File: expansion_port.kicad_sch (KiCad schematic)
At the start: 1 part, among them J2 Conn_02x30_Odd_Even

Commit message: rearrange components for routing
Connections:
- net Q3: no longer names the net of J2.35 (Pin_35)
- net Q4: no longer names the net of J2.37 (Pin_37)
- net Q5: no longer names the net of J2.39 (Pin_39)
- net Q6: no longer names the net of J2.41 (Pin_41)
- net Q7: no longer names the net of J2.43 (Pin_43)
- no-connect marks 9 -> 14
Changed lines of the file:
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@@
   (no_connect (at 78.994 36.576))
   (no_connect (at 56.134 36.576))
+  (no_connect (at 66.294 36.576))
+  (no_connect (at 68.834 36.576))
+  (no_connect (at 58.674 36.576))
+  (no_connect (at 61.214 36.576))
+  (no_connect (at 63.754 36.576))
   (no_connect (at 45.974 36.576))
   (no_connect (at 106.934 36.576))
@@
     )
   )
-  (global_label "Q6" (shape input) (at 61.214 36.576 90) (fields_autoplaced)
-    (effects (font (size 1.27 1.27)) (justify left))
-    (property "Intersheet References" "${INTERSHEET_REFS}" (id 0) (at 61.2934 31.6229 90)
-      (effects (font (size 1.27 1.27)) (justify left) hide)
-    )
-  )
   (global_label "~{E}" (shape input) (at 104.394 36.576 90) (fields_autoplaced)
     (effects (font (size 1.27 1.27)) (justify left))
@@
     )
   )
-  (global_label "Q5" (shape input) (at 63.754 36.576 90) (fields_autoplaced)
-    (effects (font (size 1.27 1.27)) (justify left))
-    (property "Intersheet References" "${INTERSHEET_REFS}" (id 0) (at 63.8334 31.6229 90)
-      (effects (font (size 1.27 1.27)) (justify left) hide)
-    )
-  )
   (global_label "~{DMA}" (shape input) (at 53.594 36.576 90) (fields_autoplaced)
     (effects (font (size 1.27 1.27)) (justify left))
@@
     )
   )
-  (global_label "Q3" (shape input) (at 68.834 36.576 90) (fields_autoplaced)
-    (effects (font (size 1.27 1.27)) (justify left))
-    (property "Intersheet References" "${INTERSHEET_REFS}" (id 0) (at 68.9134 31.6229 90)
-      (effects (font (size 1.27 1.27)) (justify left) hide)
-    )
-  )
   (global_label "~{NMI}" (shape input) (at 53.594 49.276 270) (fields_autoplaced)
     (effects (font (size 1.27 1.27)) (justify right))
@@
     )
   )
-  (global_label "Q4" (shape input) (at 66.294 36.576 90) (fields_autoplaced)
-    (effects (font (size 1.27 1.27)) (justify left))
-    (property "Intersheet References" "${INTERSHEET_REFS}" (id 0) (at 66.3734 31.6229 90)
-      (effects (font (size 1.27 1.27)) (justify left) hide)
-    )
-  )
   (global_label "A13" (shape input) (at 66.294 49.276 270) (fields_autoplaced)
     (effects (font (size 1.27 1.27)) (justify right))
@@
       (effects (font (size 1.27 1.27)) (justify left) hide)
     )
-  )
-  (global_label "Q7" (shape input) (at 58.674 36.576 90) (fields_autoplaced)
-    (effects (font (size 1.27 1.27)) (justify left))
-    (property "Intersheet References" "${INTERSHEET_REFS}" (id 0) (at 58.7534 31.6229 90)
-      (effects (font (size 1.27 1.27)) (justify left) hide)
-    )

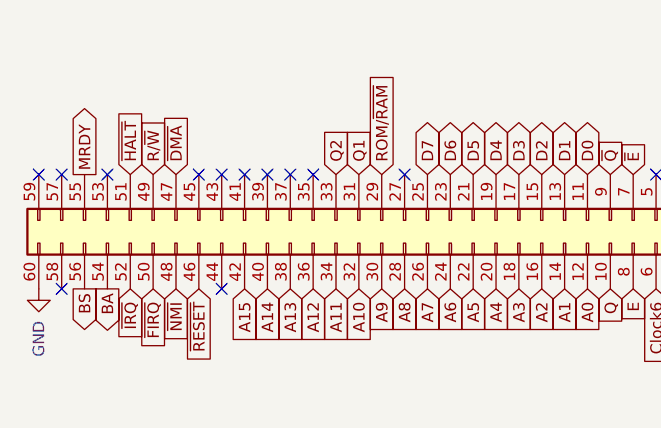
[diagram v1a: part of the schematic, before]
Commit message: correct memory page addressing
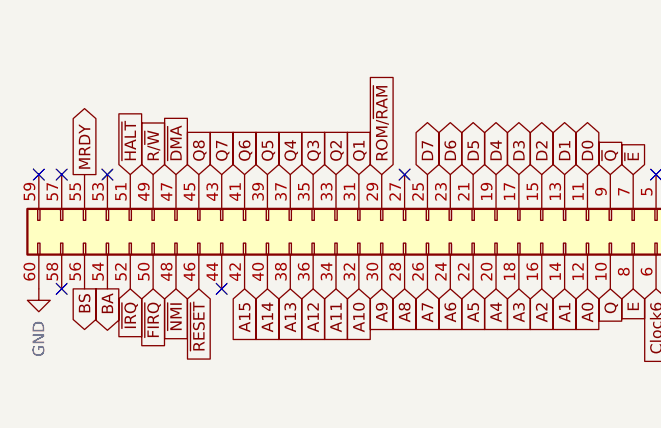
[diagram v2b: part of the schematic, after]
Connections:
- net Q3: now reaches J2.35 (Pin_35)
- net Q4: now reaches J2.37 (Pin_37)
- net Q5: now reaches J2.39 (Pin_39)
- net Q6: now reaches J2.41 (Pin_41)
- net Q7: now reaches J2.43 (Pin_43)
- net Q8: now reaches J2.45 (Pin_45)
- no-connect marks 14 -> 8
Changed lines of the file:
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@@
   (no_connect (at 112.014 36.576))
   (no_connect (at 78.994 36.576))
-  (no_connect (at 56.134 36.576))
-  (no_connect (at 66.294 36.576))
-  (no_connect (at 68.834 36.576))
-  (no_connect (at 58.674 36.576))
-  (no_connect (at 61.214 36.576))
-  (no_connect (at 63.754 36.576))
   (no_connect (at 45.974 36.576))
   (no_connect (at 106.934 36.576))
@@
     )
   )
+  (global_label "Q7" (shape input) (at 58.674 36.576 90) (fields_autoplaced)
+    (effects (font (size 1.27 1.27)) (justify left))
+    (property "Intersheet References" "${INTERSHEET_REFS}" (id 0) (at 58.5946 31.6229 90)
+      (effects (font (size 1.27 1.27)) (justify left) hide)
+    )
+  )
   (global_label "~{Q}" (shape input) (at 101.854 36.576 90) (fields_autoplaced)
     (effects (font (size 1.27 1.27)) (justify left))
@@
     )
   )
+  (global_label "Q4" (shape input) (at 66.294 36.576 90) (fields_autoplaced)
+    (effects (font (size 1.27 1.27)) (justify left))
+    (property "Intersheet References" "${INTERSHEET_REFS}" (id 0) (at 66.2146 31.6229 90)
+      (effects (font (size 1.27 1.27)) (justify left) hide)
+    )
+  )
   (global_label "~{DMA}" (shape input) (at 53.594 36.576 90) (fields_autoplaced)
     (effects (font (size 1.27 1.27)) (justify left))
@@
     )
   )
+  (global_label "Q8" (shape input) (at 56.134 36.576 90) (fields_autoplaced)
+    (effects (font (size 1.27 1.27)) (justify left))
+    (property "Intersheet References" "${INTERSHEET_REFS}" (id 0) (at 56.0546 31.6229 90)
+      (effects (font (size 1.27 1.27)) (justify left) hide)
+    )
+  )
   (global_label "A3" (shape input) (at 91.694 49.276 270) (fields_autoplaced)
     (effects (font (size 1.27 1.27)) (justify right))
@@
     )
   )
+  (global_label "Q6" (shape input) (at 61.214 36.576 90) (fields_autoplaced)
+    (effects (font (size 1.27 1.27)) (justify left))
+    (property "Intersheet References" "${INTERSHEET_REFS}" (id 0) (at 61.1346 31.6229 90)
+      (effects (font (size 1.27 1.27)) (justify left) hide)
+    )
+  )
   (global_label "A7" (shape input) (at 81.534 49.276 270) (fields_autoplaced)
     (effects (font (size 1.27 1.27)) (justify right))
@@
     )
   )
+  (global_label "Q3" (shape input) (at 68.834 36.576 90) (fields_autoplaced)
+    (effects (font (size 1.27 1.27)) (justify left))
+    (property "Intersheet References" "${INTERSHEET_REFS}" (id 0) (at 68.7546 31.6229 90)
+      (effects (font (size 1.27 1.27)) (justify left) hide)
+    )
+  )
   (global_label "A14" (shape input) (at 63.754 49.276 270) (fields_autoplaced)
     (effects (font (size 1.27 1.27)) (justify right))
@@
     )
   )
+  (global_label "Q5" (shape input) (at 63.754 36.576 90) (fields_autoplaced)
+    (effects (font (size 1.27 1.27)) (justify left))
+    (property "Intersheet References" "${INTERSHEET_REFS}" (id 0) (at 63.6746 31.6229 90)
+      (effects (font (size 1.27 1.27)) (justify left) hide)
+    )
+  )

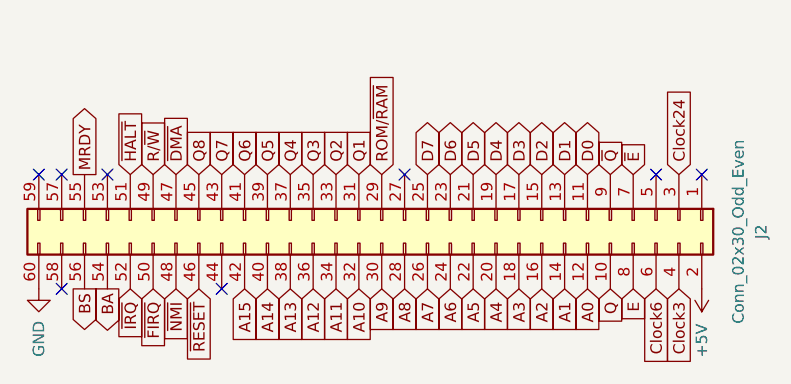
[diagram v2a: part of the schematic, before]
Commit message: modify address logic for mapped registers
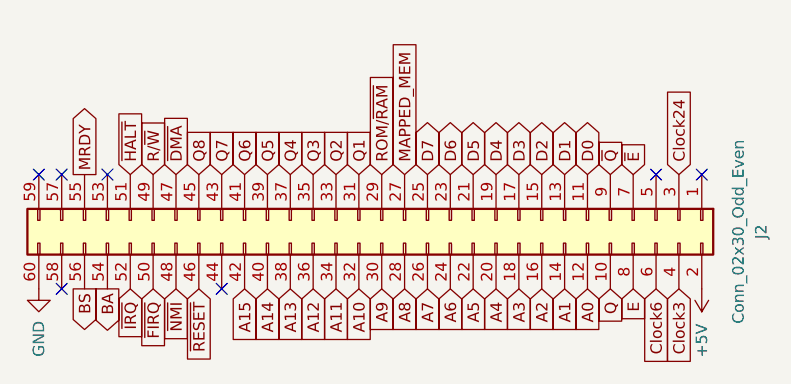
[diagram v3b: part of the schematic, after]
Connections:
- net MAPPED_MEM: now reaches J2.27 (Pin_27)
- no-connect marks 8 -> 7
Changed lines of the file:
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@@
   (paper "A4")
   (no_connect (at 112.014 36.576))
-  (no_connect (at 78.994 36.576))
   (no_connect (at 45.974 36.576))
   (no_connect (at 106.934 36.576))
@@
     )
   )
+  (global_label "MAPPED_MEM" (shape input) (at 78.994 36.576 90) (fields_autoplaced)
+    (effects (font (size 1.27 1.27)) (justify left))
+    (property "Intersheet References" "${INTERSHEET_REFS}" (id 0) (at 78.9146 21.6443 90)
+      (effects (font (size 1.27 1.27)) (justify left) hide)
+    )
+  )

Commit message: convert to new format
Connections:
- net Clock12: now reaches J2.5 (Pin_5)
- net MAPPED_MEM renamed SELPA
- net MRDY renamed AVMA
- net Q1 renamed SELPC
- net Q2 renamed SELPD
- net Q3 renamed SELPE
- net Q4 renamed SELPF
- net Q5 renamed SELPG
- net Q6 renamed SELPH
- net Q7: no longer names the net of J2.43 (Pin_43)
- net Q8: no longer names the net of J2.45 (Pin_45)
- net ROM/~{RAM} renamed SELPB
- net ~{DMA} renamed BUSY
- no-connect marks 7 -> 8
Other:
- title: (none) -> HD6309 Homebrew SBC
- moved on the sheet: J2

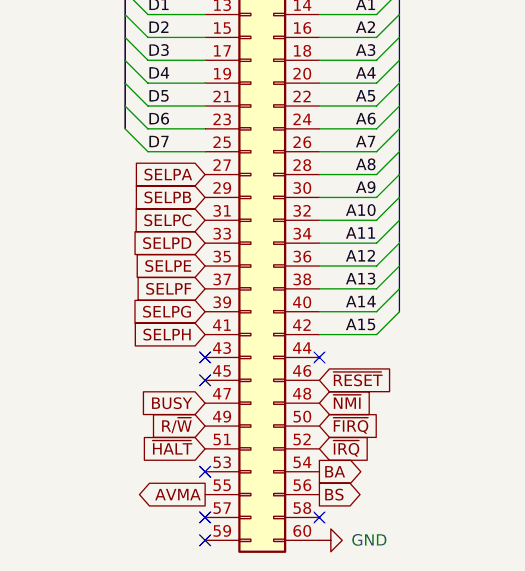
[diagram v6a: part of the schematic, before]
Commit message: disambiguate register address
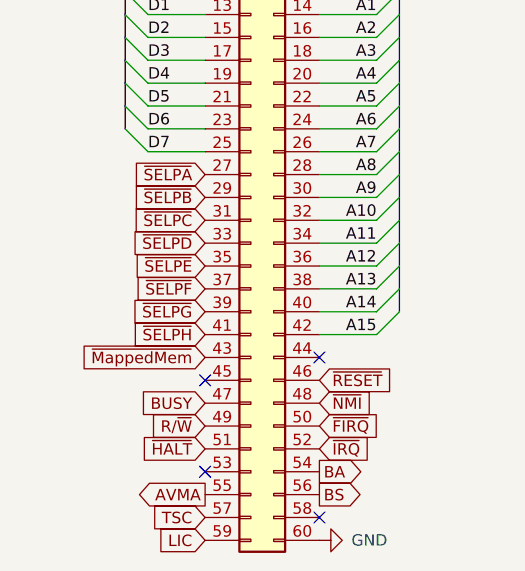
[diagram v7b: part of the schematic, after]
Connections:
- net ~{MappedMem}: now reaches J2.43 (Pin_43)
- net TSC: now reaches J2.57 (Pin_57)
- net LIC: now reaches J2.59 (Pin_59)
- net SELPA renamed ~{SELPA}
- net SELPB renamed ~{SELPB}
- net SELPC renamed ~{SELPC}
- net SELPD renamed ~{SELPD}
- net SELPE renamed ~{SELPE}
- net SELPF renamed ~{SELPF}
- net SELPG renamed ~{SELPG}
- net SELPH renamed ~{SELPH}
- no-connect marks 8 -> 5
